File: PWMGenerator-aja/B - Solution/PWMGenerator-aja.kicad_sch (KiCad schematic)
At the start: 31 parts, among them J1 Conn_01x03_Pin, Q1 2N3904, Q2 2N3904, Q3 2N3906, Q4 2N3906, SW1 SW_SPST, U1 LM7805_TO220, U2 LM339

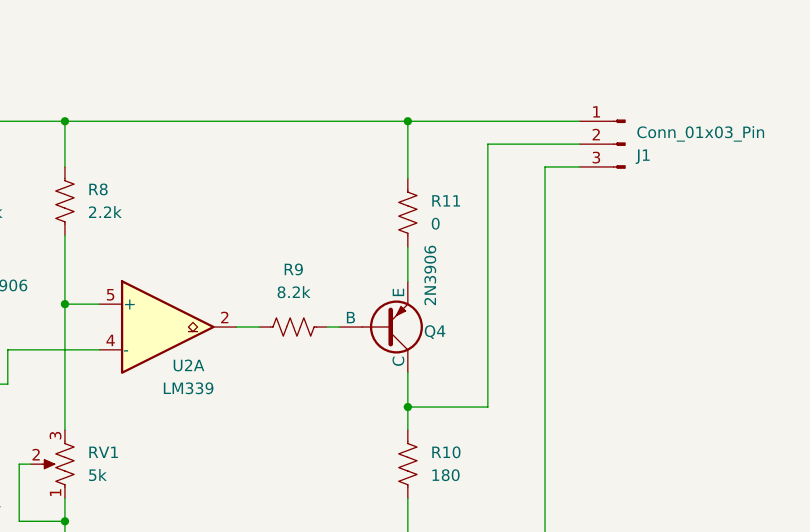
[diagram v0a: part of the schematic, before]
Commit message: Correcting minor error.  Replace solution files.
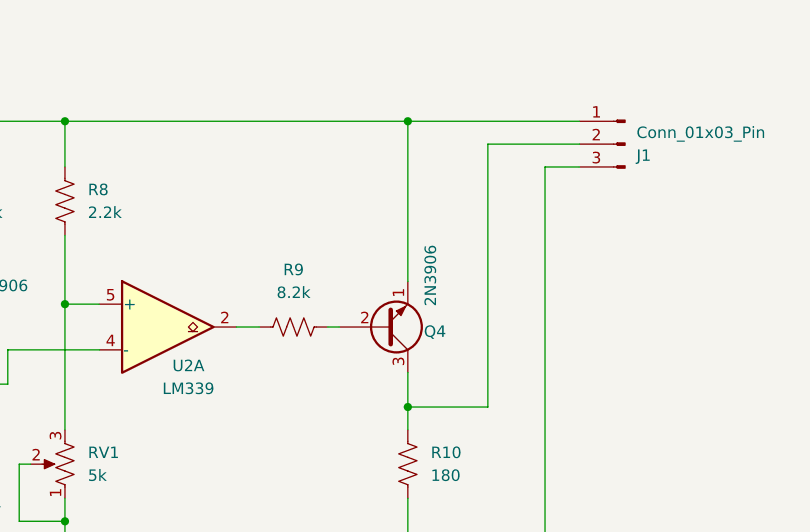
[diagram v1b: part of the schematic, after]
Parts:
- removed R11: 0, Resistor_SMD:R_0805_2012Metric, symbol Device:R_US
- Q4: footprint Package_TO_SOT_SMD:SOT-23 -> Package_TO_SOT_THT:TO-92_Inline; symbol Simulation_SPICE:PNP -> Transistor_BJT:2N3904
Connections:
- net VCC: now also Q4.1 (E)
- net at Q4.3 (C): now also J1.2 (Pin_2), R10.1
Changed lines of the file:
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@@
 	(wire
 		(pts
-			(xy 222.25 67.31) (xy 222.25 73.66)
+			(xy 222.25 67.31) (xy 222.25 85.09)
 		)
 		(stroke
@@
 		(pts
 			(xy 62.23 83.82) (xy 62.23 86.36)
-		)
-		(stroke
-			(width 0)
-			(type default)
-		)
-	)
-	(wire
-		(pts
-			(xy 222.25 81.28) (xy 222.25 85.09)
 		)
 		(stroke
@@
 	(symbol
 		(lib_id "Device:R_US")
-		(at 222.25 77.47 0)
-		(unit 1)
-		(exclude_from_sim no)
-		(in_bom yes)
-		(on_board yes)
-		(dnp no)
-		(fields_autoplaced yes)
-		(property "Reference" "R11"
-			(at 224.79 76.1999 0)
-			(effects
-				(font
-					(size 1.27 1.27)
-				)
-				(justify left)
-			)
-		)
-		(property "Value" "0"
-			(at 224.79 78.7399 0)
-			(effects
-				(font
-					(size 1.27 1.27)
-				)
-				(justify left)
-			)
-		)
-		(property "Footprint" "Resistor_SMD:R_0805_2012Metric"
-			(at 223.266 77.724 90)
-			(effects
-				(font
-					(size 1.27 1.27)
-				)
-				(hide yes)
-			)
-		)
-		(property "Datasheet" "~"
-			(at 222.25 77.47 0)
-			(effects
-				(font
-					(size 1.27 1.27)
-				)
-				(hide yes)
-			)
-		)
-		(property "Description" "Resistor, US symbol"
-			(at 222.25 77.47 0)
-			(effects
-				(font
-					(size 1.27 1.27)
-				)
-				(hide yes)
-			)
-		)
-		(pin "1"
-		)
-		(pin "2"
-		)
-		(instances
-			(project "PWMGenerator-aja"
-				(path "/18199a25-5472-4b5c-b90a-fcfdecd0a2ee"
-					(reference "R11")
-					(unit 1)
-				)
-			)
-		)
-	)
-	(symbol
-		(lib_id "Device:R_US")
 		(at 171.45 76.2 180)
 		(unit 1)
@@
 	)
 	(symbol
-		(lib_id "Simulation_SPICE:PNP")
+		(lib_id "Transistor_BJT:2N3904")
 		(at 219.71 90.17 0)
 		(mirror x)
@@
 			)
 		)
-		(property "Footprint" "Package_TO_SOT_SMD:SOT-23"
-			(at 255.27 90.17 0)
-			(effects
-				(font
-					(size 1.27 1.27)
-				)
-				(hide yes)
-			)
-		)
-		(property "Datasheet" "https://www.onsemi.com/pub/Collateral/2N3906-D.PDF"
-			(at 255.27 90.17 0)
-			(effects
-				(font
-					(size 1.27 1.27)
-				)
-				(hide yes)
-			)
-		)
-		(property "Description" "Bipolar transistor symbol for simulation only, substrate tied to the emitter"
+		(property "Footprint" "Package_TO_SOT_THT:TO-92_Inline"
+			(at 224.79 88.265 0)
+			(effects
+				(font
+					(size 1.27 1.27)
+					(italic yes)
+				)
+				(justify left)
+				(hide yes)
+			)
+		)
+		(property "Datasheet" "https://www.onsemi.com/pub/Collateral/2N3903-D.PDF"
 			(at 219.71 90.17 0)
 			(effects
+				(font
+					(size 1.27 1.27)
+				)
+				(justify left)
+				(hide yes)
+			)
+		)
+		(property "Description" "0.2A Ic, 40V Vce, Small Signal NPN Transistor, TO-92"
+			(at 219.71 90.17 0)
+			(effects

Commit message: Work on component placement
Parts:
- removed #PWR01: 12V RMS, symbol Connector:Barrel_Jack
- added J2: Barrel_Jack, Connector_BarrelJack:BarrelJack_SwitchcraftConxall_RAPC10U_Horizontal, symbol Connector:Barrel_Jack
- D6: value LED Green -> LED; footprint LED_THT:LED_D5.0mm_Green -> LED_THT:LED_D5.0mm
- F1: footprint local:RESC3115X65N -> lib:RESC3115X65N
- Q2, Q3, Q4: footprint Package_TO_SOT_THT:TO-92_Inline -> Package_TO_SOT_SMD:SOT-23
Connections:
- net GNDPWR: now also J2.2
- net at SW1.1 (A): now also J2.1
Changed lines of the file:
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@@
 			)
 		)
-		(property "Footprint" "Package_TO_SOT_THT:TO-92_Inline"
+		(property "Footprint" "Package_TO_SOT_SMD:SOT-23"
 			(at 224.79 88.265 0)
 			(effects
@@
 			)
 		)
-		(property "Datasheet" "https://www.onsemi.com/pub/Collateral/2N3903-D.PDF"
+		(property "Datasheet" "https://www.onsemi.com/pub/Collateral/2N3906-D.PDF"
 			(at 219.71 90.17 0)
 			(effects
@@
 	)
 	(symbol
+		(lib_id "Connector:Barrel_Jack")
+		(at 22.86 93.98 0)
+		(unit 1)
+		(exclude_from_sim no)
+		(in_bom yes)
+		(on_board yes)
+		(dnp no)
+		(fields_autoplaced yes)
+		(property "Reference" "J2"
+			(at 22.86 85.09 0)
+			(effects
+				(font
+					(size 1.27 1.27)
+				)
+			)
+		)
+		(property "Value" "Barrel_Jack"
+			(at 22.86 87.63 0)
+			(effects
+				(font
+					(size 1.27 1.27)
+				)
+			)
+		)
+		(property "Footprint" "Connector_BarrelJack:BarrelJack_SwitchcraftConxall_RAPC10U_Horizontal"
+			(at 24.13 94.996 0)
+			(effects
+				(font
+					(size 1.27 1.27)
+				)
+				(hide yes)
+			)
+		)
+		(property "Datasheet" "~"
+			(at 24.13 94.996 0)
+			(effects
+				(font
+					(size 1.27 1.27)
+				)
+				(hide yes)
+			)
+		)
+		(property "Description" "DC Barrel Jack"
+			(at 22.86 93.98 0)
+			(effects
+				(font
+					(size 1.27 1.27)
+				)
+				(hide yes)
+			)
+		)
+		(pin "1"
+		)
+		(pin "2"
+		)
+		(instances
+			(project ""
+				(path "/18199a25-5472-4b5c-b90a-fcfdecd0a2ee"
+					(reference "J2")
+					(unit 1)
+				)
+			)
+		)
+	)
+	(symbol
 		(lib_id "Device:R_US")
 		(at 135.89 76.2 180)
@@
 			)
 		)
-		(property "Footprint" "local:RESC3115X65N"
+		(property "Footprint" "lib:RESC3115X65N"
 			(at 53.34 66.04 0)
 			(effects
@@
 			)
 		)
-		(property "Value" "LED Green"
+		(property "Value" "LED"
 			(at 127 108.2674 90)
 			(effects
@@
 			)
 		)
-		(property "Footprint" "LED_THT:LED_D5.0mm_Green"
+		(property "Footprint" "LED_THT:LED_D5.0mm"
 			(at 123.19 105.41 0)
 			(effects
@@
 	)
 	(symbol
-		(lib_id "Connector:Barrel_Jack")
-		(at 22.86 93.98 0)
-		(unit 1)
-		(exclude_from_sim no)
-		(in_bom yes)
-		(on_board yes)
-		(dnp no)
-		(property "Reference" "#PWR01"
-			(at 22.86 96.52 0)
-			(effects
-				(font
-					(size 1.27 1.27)
-				)
-				(hide yes)
-			)
-		)
-		(property "Value" "12V RMS"
-			(at 26.67 88.646 0)
-			(effects
-				(font
-					(size 1.27 1.27)
-				)
-				(justify right)
-			)
-		)
-		(property "Footprint" ""
-			(at 24.13 94.996 0)
-			(effects
-				(font
-					(size 1.27 1.27)
-				)
-				(hide yes)
-			)
-		)
-		(property "Datasheet" "~"
-			(at 24.13 94.996 0)
-			(effects
-				(font
-					(size 1.27 1.27)
-				)
-				(hide yes)
-			)
-		)
-		(property "Description" "DC Barrel Jack"
-			(at 22.86 93.98 0)
-			(effects
-				(font
-					(size 1.27 1.27)
-				)
-				(hide yes)
-			)
-		)
-		(property "Sim.Pins" "1=+ 2=-"
-			(at 22.86 93.98 0)
-			(effects
-				(font
-					(size 1.27 1.27)
-				)
-				(hide yes)
-			)
-		)
-		(property "Sim.Params" "dc=0 ampl=1 f=1k ac=1"
-			(at 19.05 95.1201 0)
-			(effects
-				(font
-					(size 1.27 1.27)
-				)
-				(justify right)
-				(hide yes)
-			)
-		)
-		(property "Sim.Type" "SIN"
-			(at 22.86 93.98 0)
-			(effects
-				(font
-					(size 1.27 1.27)
-				)
-				(hide yes)
-			)
-		)
-		(property "Sim.Device" "V"
-			(at 22.86 93.98 0)
-			(effects
-				(font
-					(size 1.27 1.27)
-				)
-				(justify left)
-				(hide yes)
-			)
-		)
-		(pin "1"
-		)
-		(pin "2"
-		)
-		(instances
-			(project ""
-				(path "/18199a25-5472-4b5c-b90a-fcfdecd0a2ee"
-					(reference "#PWR01")
-					(unit 1)
-				)
-			)
-		)
-	)
-	(symbol
 		(lib_id "Device:C_Polarized")
 		(at 107.95 76.2 0)
@@
 			)
 		)
-		(property "Footprint" "Package_TO_SOT_THT:TO-92_Inline"
+		(property "Footprint" "Package_TO_SOT_SMD:SOT-23"
 			(at 148.59 107.315 0)
 			(effects
@@
 			)
 		)
-		(property "Datasheet" "https://www.onsemi.com/pub/Collateral/2N3906-D.PDF"
+		(property "Datasheet" "https://www.onsemi.com/pdf/datasheet/pzt3904-d.pdf"
 			(at 143.51 105.41 0)
 			(effects
@@
 			)
 		)
-		(property "Datasheet" "https://www.onsemi.com/pub/Collateral/2N3903-D.PDF"
+		(property "Datasheet" "https://www.onsemi.com/pdf/datasheet/pzt3904-d.pdf"
 			(at 105.41 101.6 0)
 			(effects
@@
 			)
 		)
-		(property "Footprint" "Package_TO_SOT_THT:TO-92_Inline"
+		(property "Footprint" "Package_TO_SOT_SMD:SOT-23"
 			(at 204.47 87.63 0)
 			(effects
@@
 			)
 		)
-		(property "Datasheet" "https://ngspice.sourceforge.io/docs/ngspice-html-manual/manual.xhtml#cha_BJTs"
+		(property "Datasheet" "https://www.onsemi.com/pub/Collateral/2N3906-D.PDF"
 			(at 204.47 87.63 0)
 			(effects
